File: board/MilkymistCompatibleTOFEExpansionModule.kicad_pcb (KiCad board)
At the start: 2 copper layers, 110 x 111.3 mm, 118 parts, among them CON1 AUDIO_JACK_3535NG, CON2 AUDIO_JACK_3535NG, CON3 AUDIO_JACK_3535NG, CON4 AUDIO_JACK_3535NG, IC1 PC817, J1 DB9, K1 CONN_2, K2 CONN_2, K3 CONN_3, K4 CONN_3, K5 CONN_2, K6 CONN_2, K7 CONN_2, K8 CONN_2, P2 CONN_4X2, P4 CONN_6X2, P5 CONN_6X2, Q1 TRANSISTOR-NPN, SW1 SW_PUSH, SW2 SW_PUSH, SW3 SW_PUSH, SW4 SW_PUSH, U1 LM4550, U2 7805_N, U3 ST3232CDR, U4 SN74LVC1G17, U5 ISL83490, U6 IR-RX, U7 24AA01/24LC01B, U8 TIMVIDEOS-PCIE-8X, X1 CRYSTAL

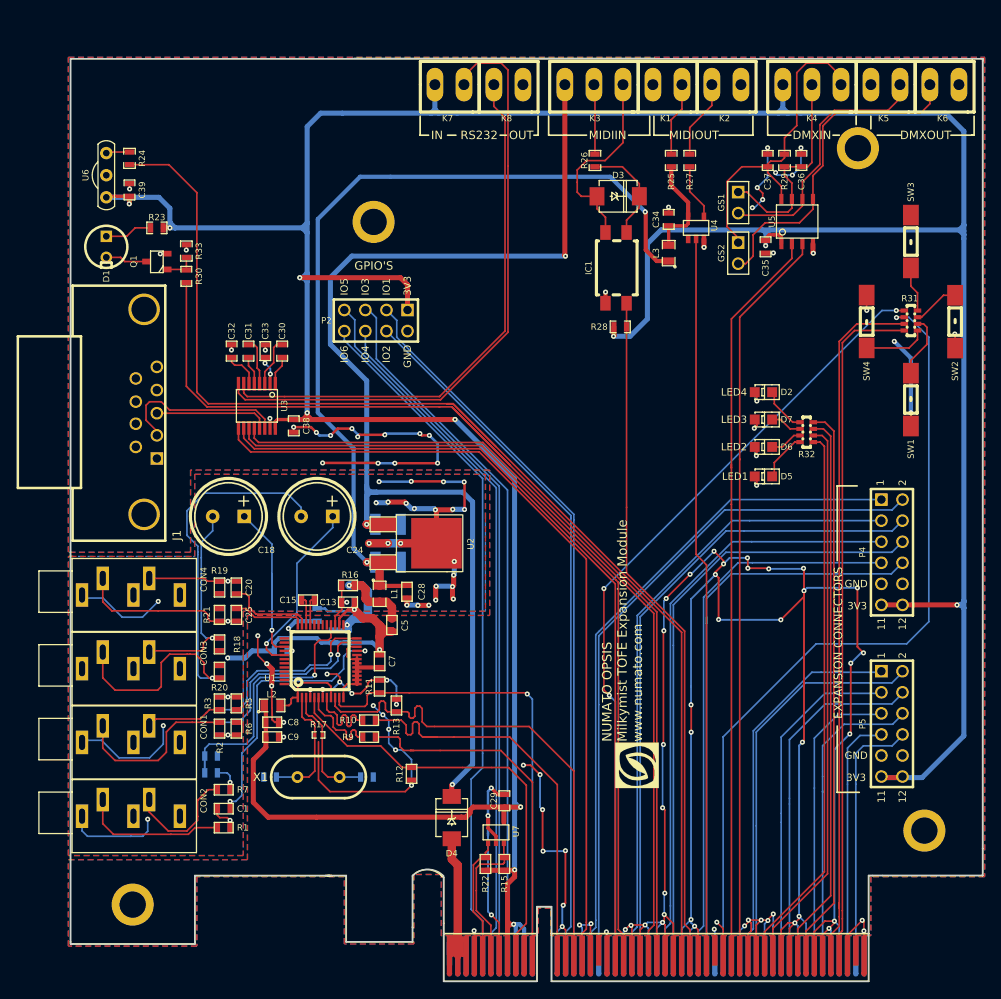
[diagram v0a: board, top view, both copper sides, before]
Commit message: changes on Mounting holes arrangement
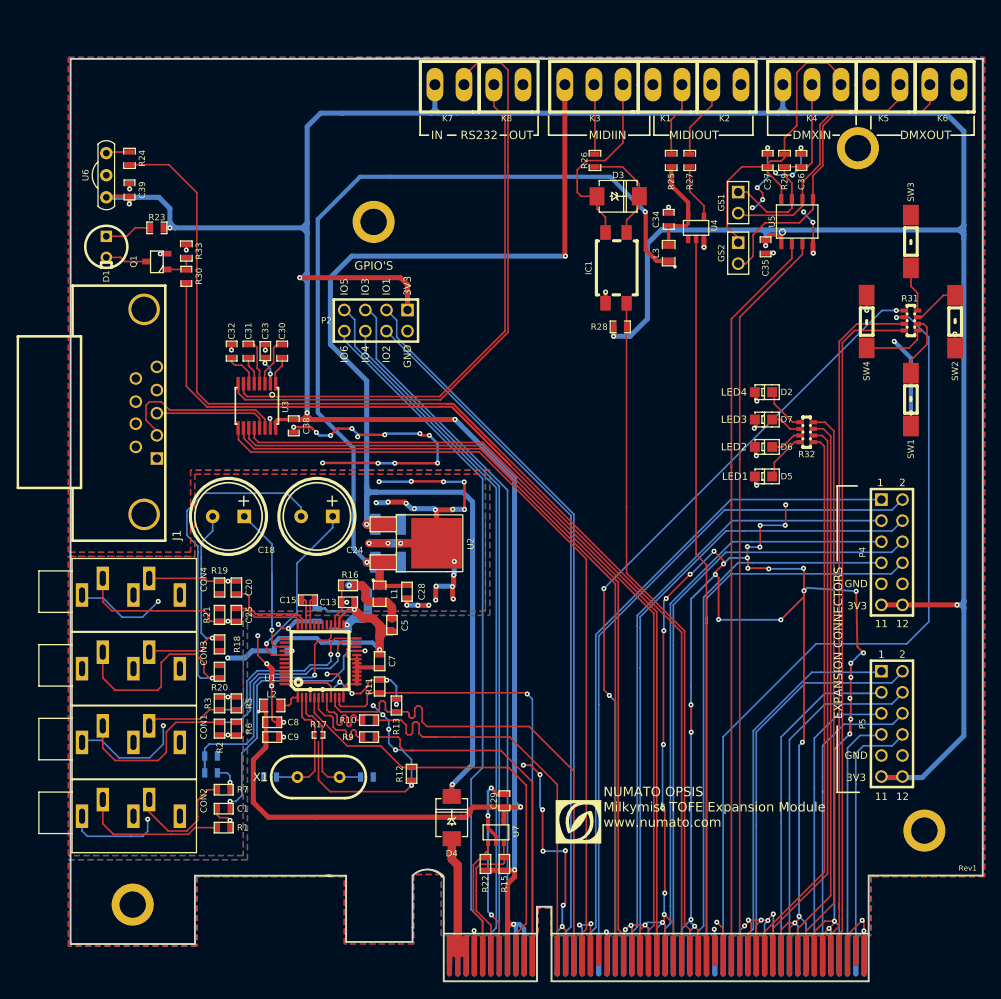
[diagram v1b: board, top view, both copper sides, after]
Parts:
- removed 1PIN (x2): P***, MH-4MM
- U3: footprint ssop-16 -> TSSOP-16
- moved G*** 9.88 mm to (149.4, 129.0), turned to 0 degrees
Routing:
- net /GND: track 568.0 -> 596.1 mm, vias 113 -> 124
- net /12V: track 31.8 -> 36.4 mm
- net /GPIO2: track 84.7 -> 87.0 mm
- net /AC97_SDI: track 51.3 -> 53.6 mm
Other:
- board text added: "Rev1"

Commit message: Mechanical hole changes
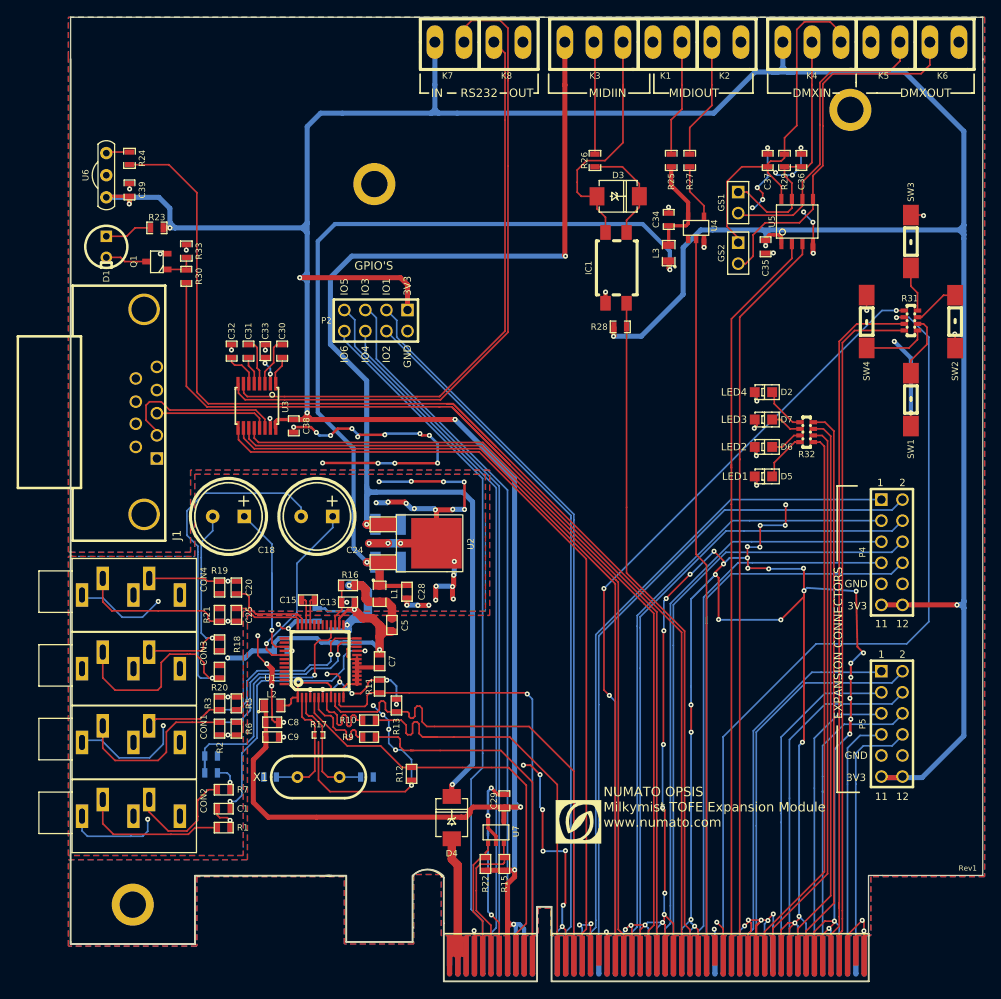
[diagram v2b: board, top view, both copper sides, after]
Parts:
- U8: footprint NumatoOpsis_PCIe_8X_HL_NW_110x110 -> NumatoOpsis_PCIe_8X_HL_NW_1
- moved U8 57.3 mm to (145.3, 148.3)
- moved K1 5.13 mm to (158.4, 35.0)
- moved K2 5.13 mm to (165.5, 35.0)
- moved K3 5.13 mm to (151.3, 35.0)
- moved K4 5.13 mm to (177.5, 35.0)
- moved K5 5.13 mm to (184.7, 35.0)
- moved K6 5.13 mm to (191.8, 35.0)
- moved K7 5.13 mm to (132.1, 35.0)
- moved K8 5.13 mm to (139.2, 35.0)
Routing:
- net /GND: track 596.1 -> 690.0 mm, vias 124 -> 125
- net /VCC3V3: track 492.0 -> 510.0 mm
- net /12V: track 36.4 -> 47.9 mm
- net /MIDI_IN_PIN5: track 23.9 -> 30.0 mm
- net /VCC5V0: track 104.4 -> 98.4 mm
- net /RS232-IN2: track 76.3 -> 81.8 mm
- net /DMX-DATA_OUT-: track 31.6 -> 37.1 mm
- net /DMX-DATA_OUT+: track 40.1 -> 45.5 mm
- net /DMX-DATA_IN-: track 25.9 -> 31.2 mm
- net /VCC12V: track 141.5 -> 146.7 mm
- net /MIDI_OUT_PIN4: track 8.92 -> 14.1 mm
- net /MIDI_OUT_PIN5: track 9.49 -> 14.6 mm
- net /MIDI_IN_PIN4: track 8.43 -> 13.6 mm
- net /RS232-OUT2: track 66.4 -> 71.5 mm
- net /DMX-DATA_IN+: track 39.2 -> 44.3 mm
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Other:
- board size 110 x 111.3 mm -> 110 x 116.3 mm
